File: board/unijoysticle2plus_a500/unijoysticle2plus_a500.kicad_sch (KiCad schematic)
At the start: 0 parts

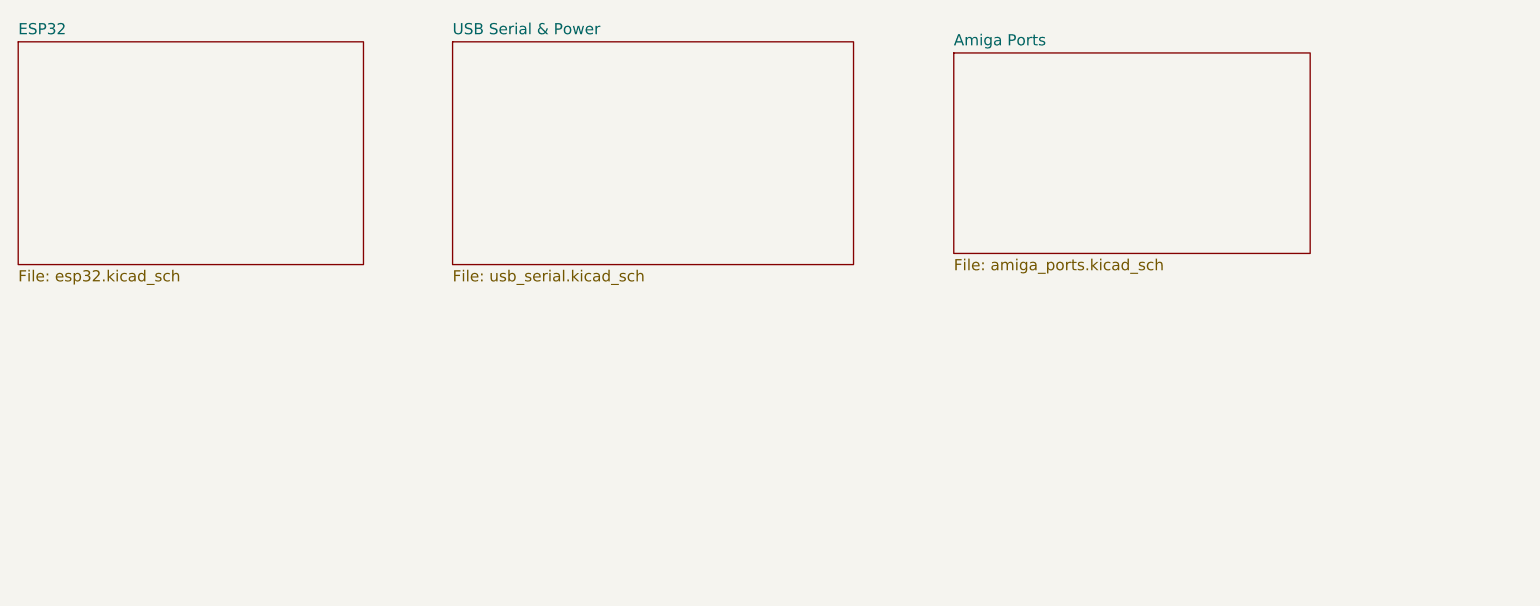
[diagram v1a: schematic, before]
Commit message: uni2+ a500: schematic "ready"
The schematic should be "ready".
Layout WIP. Components were placed in "place".
But routing is missing, as well as logos
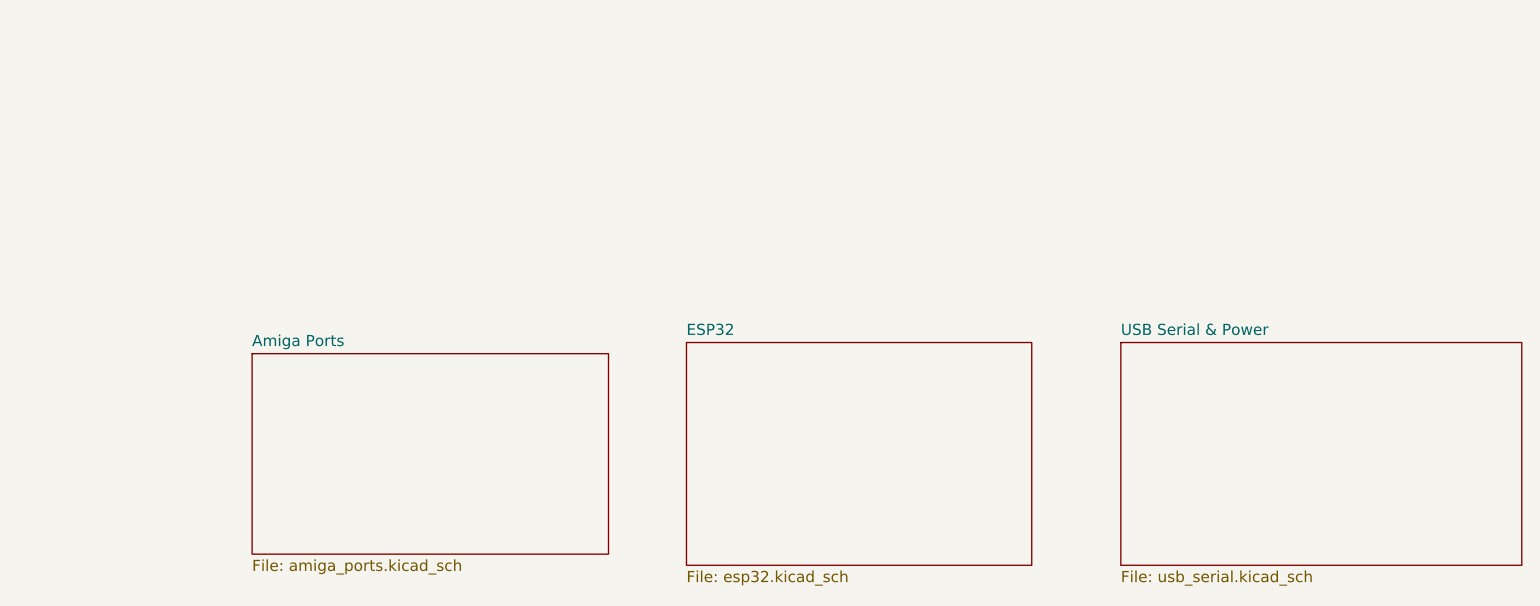
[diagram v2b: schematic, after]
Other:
- title: Unijoysticle 2+ -> Unijoysticle 2+ A500

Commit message: Rename Uni2+ A500 to Uni2 A500
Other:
- title: Unijoysticle 2+ A500 -> Unijoysticle 2 A500
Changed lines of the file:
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@@
   (paper "A4")
   (title_block
-    (title "Unijoysticle 2+ A500")
-    (date "2022-04-20")
+    (title "Unijoysticle 2 A500")
+    (date "2022-04-25")
     (rev "A")
     (company "Retro Moe")
